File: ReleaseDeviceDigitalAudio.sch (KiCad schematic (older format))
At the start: 11 parts, among them J1 AudioJack3, J2 AudioJack3, J3 AudioJack3, J4 AudioJack3, J5 AudioJack3

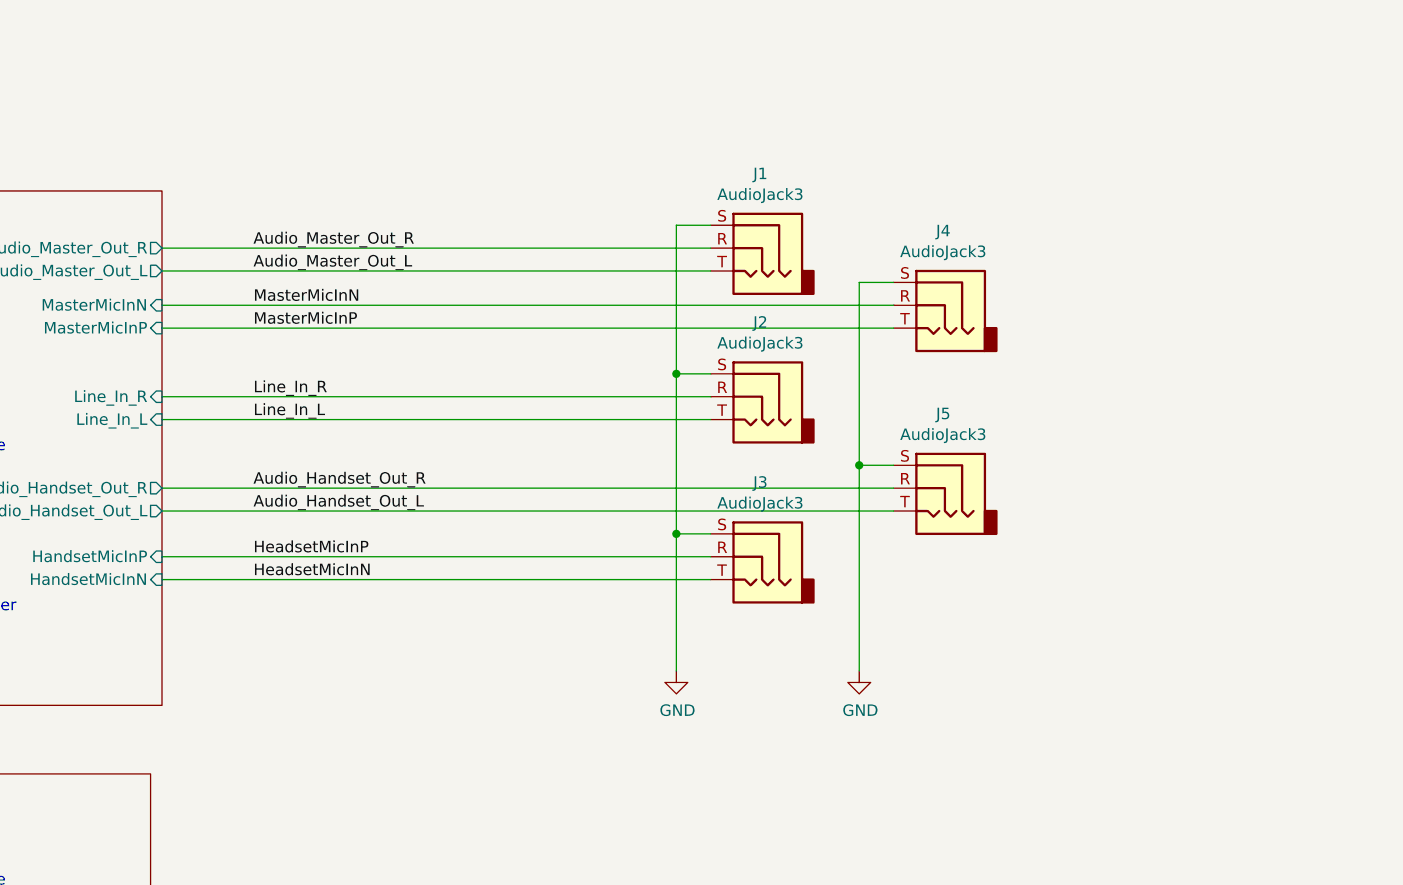
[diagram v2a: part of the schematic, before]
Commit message: - neue Stecker hinzugefügt, Annotation überall entsprechend angepasst Footprint fehlt noch
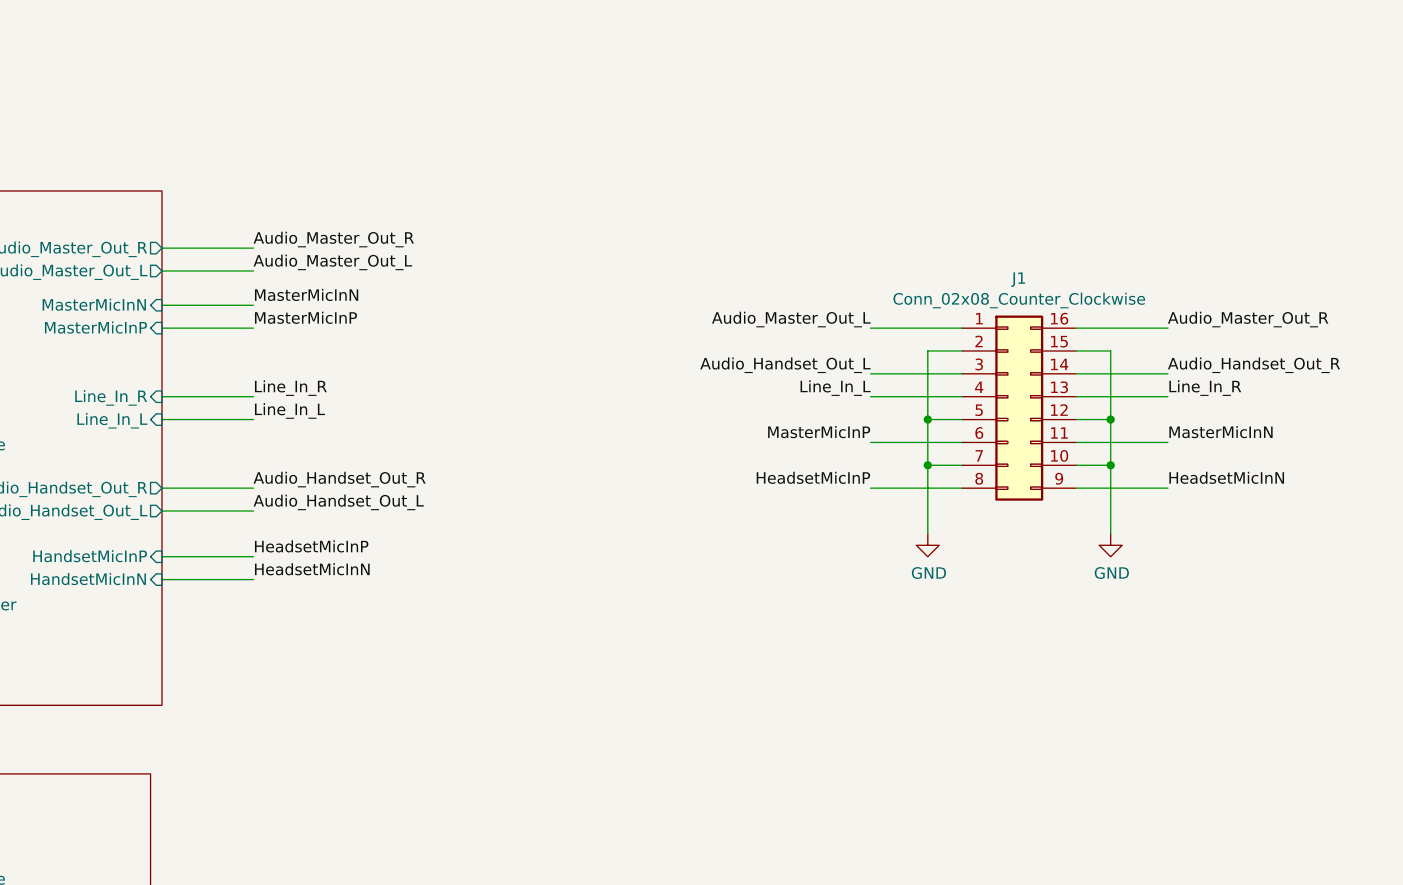
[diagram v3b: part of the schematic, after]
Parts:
- removed J1, J2, J3, J4, J5: AudioJack3, TeKaDe:LumbergKLB4, symbol Connector:AudioJack3
- added J1: Conn_02x08_Counter_Clockwise, Connector_PinSocket_2.00mm:PinSocket_2x07_P2.00mm_Vertical, symbol Connector_Generic:Conn_02x08_Counter_Clockwise
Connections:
- net Audio_Handset_Out_L: now also J1.3 (Pin_3)
- net Audio_Handset_Out_R: now also J1.14 (Pin_14)
- net Audio_Master_Out_L: now also J1.1 (Pin_1)
- net Audio_Master_Out_R: now also J1.16 (Pin_16)
- net GND: now also J1.10 (Pin_10), J1.12 (Pin_12), J1.15 (Pin_15), J1.2 (Pin_2), J1.5 (Pin_5), J1.7 (Pin_7)
- net HeadsetMicInN: now also J1.9 (Pin_9)
- net HeadsetMicInP: now also J1.8 (Pin_8)
- net Line_In_L: now also J1.4 (Pin_4)
- net Line_In_R: now also J1.13 (Pin_13)
- net MasterMicInN: now also J1.11 (Pin_11)
- net MasterMicInP: now also J1.6 (Pin_6)
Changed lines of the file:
@@
 L power:GND #PWR02
 U 1 1 62252CE5
-P 12700 3200
-F 0 "#PWR02" H 12700 2950 50  0001 C CNN
-F 1 "GND" H 12705 3027 50  0000 C CNN
-F 2 "" H 12700 3200 50  0001 C CNN
-F 3 "" H 12700 3200 50  0001 C CNN
-	1    12700 3200
-	1    0    0    -1
-$EndComp
-$Comp
-L power:GND #PWR01
-U 1 1 622523CD
-P 11900 3200
-F 0 "#PWR01" H 11900 2950 50  0001 C CNN
-F 1 "GND" H 11905 3027 50  0000 C CNN
-F 2 "" H 11900 3200 50  0001 C CNN
-F 3 "" H 11900 3200 50  0001 C CNN
-	1    11900 3200
+P 13000 2600
+F 0 "#PWR02" H 13000 2350 50  0001 C CNN
+F 1 "GND" H 13005 2427 50  0000 C CNN
+F 2 "" H 13000 2600 50  0001 C CNN
+F 3 "" H 13000 2600 50  0001 C CNN
+	1    13000 2600
 	1    0    0    -1
 $EndComp
@@
 ToDo: \n- Auswahl Steckverbinder Analog Audio\n- Auswahl Steckverbinder KFZ (Dauerstrom / Zündung) 3Pol\n\n- Footprint Q von Dauerstrom Verpolschutz machen\n\n- BM83: Microchip Design Checklist ausfuellen, wenn Layout fertig\n\n- Battery Holder CR1220 ? Layout wirds zeigen…\n\n\nERLEDIGT:\nSelbsthaltung:\n- Verhalten GPIO output bei undervoltage lockout \n    -> Dauerhaft unter Schwelle, Pulldown R23 trotzdem sinnvoll\n- Test durch Fredrik (Simulation wäre zu aufwendig)\n\nCM4: \n- RUN PG / Global_EN Test durch Fredrik\n    -> 5V-Kompatibel -> LevelShift entfällt (GETESTET)\n- Footprint checken durch Fredrik\n    -> Passt perfekt (GETESTET)\n- Checken ob die 3,3 und 1,8V ausgänge bzgl. Ripple in Ordnung sind\n    -> Für MAX98089 ausreichend, Oszi fehlt, daher keine genauen Daten\n- Schaltfrequenz onboard Regler\n    -> 1 - 2.1 MHz (abhängig von Config)\n\nBM83\n- Unused Pin Connections nicht beschrieben \n    -> floating lassen und später Prüfung mit Design check\n- Temperatur Messung HW seitig implementieren\n   -> Fredrik kümmert sich ggf. um SW Implementierung, etc.\n- MFB wird noch getestet durch Fredrik  \n   -> nicht benötigt, da Power On/Off per UART konfigurierbar\n- MCLK-Ausgang implementiert\n- Ersetzen durch Modell mit automotive Zulassung?\n   -> Nein weiter so mit 4Layers Aussage zur Typgenehmigung\n\nMAX98089:\n- LDO für MAX98089? \n    - Test: Stromversorgung über CM: kein Noise, Load unerheblich\n- Config: Voice vs. Music filter: Done\n- MCLK-Eingang implementiert\n\nATmega:\n- Wozu 10k R an PWM Ausgang?\n   -> 1V macht Vollaussteuerung\n        Fredrik klärt PWM Frequenz, Auflöung und Eingangs-R des Zeigers\n        -> Vollausst. bei 0.22V, 0.5-1k R_innen -> 15k Vorwiderstand (GETESTET)\n        -> PER=100 -> 0,05V-Schritte, f=100kHz\n- Programmierbeschaltung ohne Reset?\n    -> check durch Fredrik -> Reset nicht benötigt\n- int. OSC checken bzgl. Kalwerte und UART Baudrate\n    -> betrifft nur SW, Bearbeitung durch Fredrik\n- Auslegung Spannungsteiler mit LDR\n    -> Standard 10k\n\nAllgemeines: \n- Levelshift prüfen (Zuordnung RX/TX)\n- Signalzuordungen I2C / I2S / UART checken\n- Abschaltung UI Board implementieren (SW6 soll 5V von UI Board schalten, LED_ON alternierend dazu\n- Zündung nur 1pol anschließen? -> kein Verpolschutz notwendig\n  (Optokoppler Eingang verträgt nur 5V reverse…)\n    -> Ja, mit 3 poligen Kombistecker\n- Auslegung Vorwiderstände an reale LEDs
 Wire Wire Line
-	9650 2400 12850 2400
-Wire Wire Line
-	9650 1700 12850 1700
-Wire Wire Line
-	9650 2800 12050 2800
-Wire Wire Line
-	9650 2700 12050 2700
-Wire Wire Line
-	9650 2500 12850 2500
-Wire Wire Line
-	9650 2100 12050 2100
-Wire Wire Line
-	9650 2000 12050 2000
-Wire Wire Line
-	9650 1600 12850 1600
-Wire Wire Line
-	9650 1450 12050 1450
-Wire Wire Line
-	9650 1350 12050 1350
+	9650 2400 10050 2400
+Wire Wire Line
+	9650 1700 10050 1700
+Wire Wire Line
+	9650 2800 10050 2800
+Wire Wire Line
+	9650 2700 10050 2700
+Wire Wire Line
+	9650 2500 10050 2500
+Wire Wire Line
+	9650 2100 10050 2100
+Wire Wire Line
+	9650 1600 10050 1600
 Wire Wire Line
 	9650 8500 10950 8500
 Wire Wire Line
 	9650 8400 10950 8400
-Wire Wire Line
-	12700 2300 12700 3200
-Connection ~ 12700 2300
-Wire Wire Line
-	12850 2300 12700 2300
-Wire Wire Line
-	11900 2600 11900 3200
-Connection ~ 11900 2600
-Wire Wire Line
-	12050 2600 11900 2600
-Wire Wire Line
-	12700 1500 12700 2300
-Wire Wire Line
-	11900 1900 11900 2600
-Connection ~ 11900 1900
 Wire Wire Line
 	8050 4900 5550 4900
@@
 Line_In_L
 Wire Wire Line
-	11900 1250 11900 1900
-Wire Wire Line
-	12050 1250 11900 1250
-Wire Wire Line
-	12050 1900 11900 1900
-Wire Wire Line
-	12850 1500 12700 1500
-$Comp
-L Connector:AudioJack3 J5
-U 1 1 6123782D
-P 13050 2400
-F 0 "J5" H 13032 2725 50  0000 C CNN
-F 1 "AudioJack3" H 13032 2634 50  0000 C CNN
-F 2 "TeKaDe:LumbergKLB4" H 13050 2400 50  0001 C CNN
-F 3 "~" H 13050 2400 50  0001 C CNN
-	1    13050 2400
-	-1   0    0    -1
-$EndComp
-$Comp
-L Connector:AudioJack3 J3
-U 1 1 6105818C
-P 12250 2700
-F 0 "J3" H 12232 3025 50  0000 C CNN
-F 1 "AudioJack3" H 12232 2934 50  0000 C CNN
-F 2 "TeKaDe:LumbergKLB4" H 12250 2700 50  0001 C CNN
-F 3 "~" H 12250 2700 50  0001 C CNN
-	1    12250 2700
-	-1   0    0    -1
-$EndComp
-$Comp
-L Connector:AudioJack3 J2
-U 1 1 6066C958
-P 12250 2000
-F 0 "J2" H 12232 2325 50  0000 C CNN
-F 1 "AudioJack3" H 12232 2234 50  0000 C CNN
-F 2 "TeKaDe:LumbergKLB4" H 12250 2000 50  0001 C CNN
-F 3 "~" H 12250 2000 50  0001 C CNN
-	1    12250 2000
-	-1   0    0    -1
-$EndComp
-$Comp
-L Connector:AudioJack3 J1
-U 1 1 60575B8C
-P 12250 1350
-F 0 "J1" H 12232 1675 50  0000 C CNN
-F 1 "AudioJack3" H 12232 1584 50  0000 C CNN
-F 2 "TeKaDe:LumbergKLB4" H 12250 1350 50  0001 C CNN
-F 3 "~" H 12250 1350 50  0001 C CNN
-	1    12250 1350
-	-1   0    0    -1
-$EndComp
-$Comp
-L Connector:AudioJack3 J4
-U 1 1 66962862
-P 13050 1600
-F 0 "J4" H 13032 1925 50  0000 C CNN
-F 1 "AudioJack3" H 13032 1834 50  0000 C CNN
-F 2 "TeKaDe:LumbergKLB4" H 13050 1600 50  0001 C CNN
-F 3 "~" H 13050 1600 50  0001 C CNN
-	1    13050 1600
-	-1   0    0    -1
-$EndComp
+	13150 1800 13000 1800
 Text Notes 4600 5800 0    50   ~ 0
 I2C Master
@@
 Wire Wire Line
 	9650 7850 10950 7850
+$Comp
+L Connector_Generic:Conn_02x08_Counter_Clockwise J1
+U 1 1 618DA775
+P 13350 2000
+F 0 "J1" H 13400 2517 50  0000 C CNN
+F 1 "Conn_02x08_Counter_Clockwise" H 13400 2426 50  0000 C CNN
+F 2 "Connector_PinSocket_2.00mm:PinSocket_2x07_P2.00mm_Vertical" H 13350 2000 50  0001 C CNN
+F 3 "~" H 13350 2000 50  0001 C CNN
+	1    13350 2000
+	1    0    0    -1
+$EndComp
+Wire Wire Line
+	9650 2000 10050 2000
+Wire Wire Line
+	9650 1350 10050 1350
+Wire Wire Line
+	12750 1700 13150 1700
+Wire Wire Line
+	9650 1450 10050 1450
+Wire Wire Line
+	13150 2200 12750 2200
+Wire Wire Line
+	13650 2400 14050 2400
+Wire Wire Line
+	13150 2400 12750 2400
+Wire Wire Line
+	13150 1900 12750 1900
+Wire Wire Line
+	13150 2000 12750 2000
+Wire Wire Line
+	13650 2200 14050 2200
+Text Label 12750 1900 2    50   ~ 0
+Audio_Handset_Out_L
+Text Label 14050 1900 0    50   ~ 0
+Audio_Handset_Out_R
+Text Label 14050 2400 0    50   ~ 0
+HeadsetMicInN
+Text Label 12750 2400 2    50   ~ 0
+HeadsetMicInP
+Text Label 12750 1700 2    50   ~ 0
+Audio_Master_Out_L
+Text Label 14050 1700 0    50   ~ 0
+Audio_Master_Out_R
+Text Label 14050 2200 0    50   ~ 0
+MasterMicInN
+Text Label 12750 2200 2    50   ~ 0
+MasterMicInP
+Text Label 14050 2000 0    50   ~ 0
+Line_In_R
+Text Label 12750 2000 2    50   ~ 0
+Line_In_L
+Wire Wire Line
+	13650 2000 14050 2000
+Wire Wire Line
+	13650 1700 14050 1700
+Wire Wire Line
+	13650 1900 14050 1900
+Wire Wire Line
+	13000 1800 13000 2100
+Wire Wire Line
+	13150 2100 13000 2100
+Connection ~ 13000 2100
+Wire Wire Line
+	13150 2300 13000 2300
+Wire Wire Line
+	13000 2100 13000 2300
+Connection ~ 13000 2300
+Wire Wire Line
+	13000 2300 13000 2600
+$Comp
+L power:GND #PWR0183
+U 1 1 6194BA95
+P 13800 2600
+F 0 "#PWR0183" H 13800 2350 50  0001 C CNN
+F 1 "GND" H 13805 2427 50  0000 C CNN
+F 2 "" H 13800 2600 50  0001 C CNN
+F 3 "" H 13800 2600 50  0001 C CNN
+	1    13800 2600
+	1    0    0    -1
+$EndComp
+Wire Wire Line
+	13650 1800 13800 1800
+Wire Wire Line
+	13800 1800 13800 2100
+Wire Wire Line
+	13650 2100 13800 2100
+Connection ~ 13800 2100
+Wire Wire Line
+	13800 2100 13800 2300
+Wire Wire Line
+	13650 2300 13800 2300
+Connection ~ 13800 2300
+Wire Wire Line
+	13800 2300 13800 2600
 $EndSCHEMATC
